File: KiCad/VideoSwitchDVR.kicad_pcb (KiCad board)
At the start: 2 copper layers, 18 x 25 mm, 7 parts, among them SW1 Joystick, U1 ATTINY84-20MU, U2 MAX4624/5

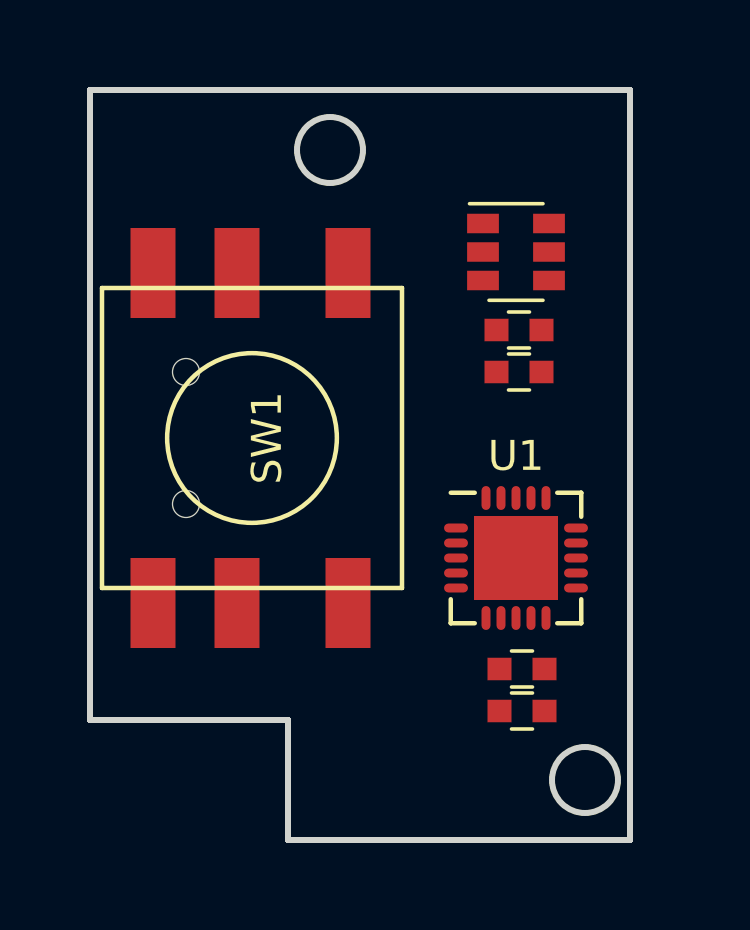
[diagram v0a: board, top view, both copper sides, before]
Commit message: Some progress on PCB. MCU changed to simplier one
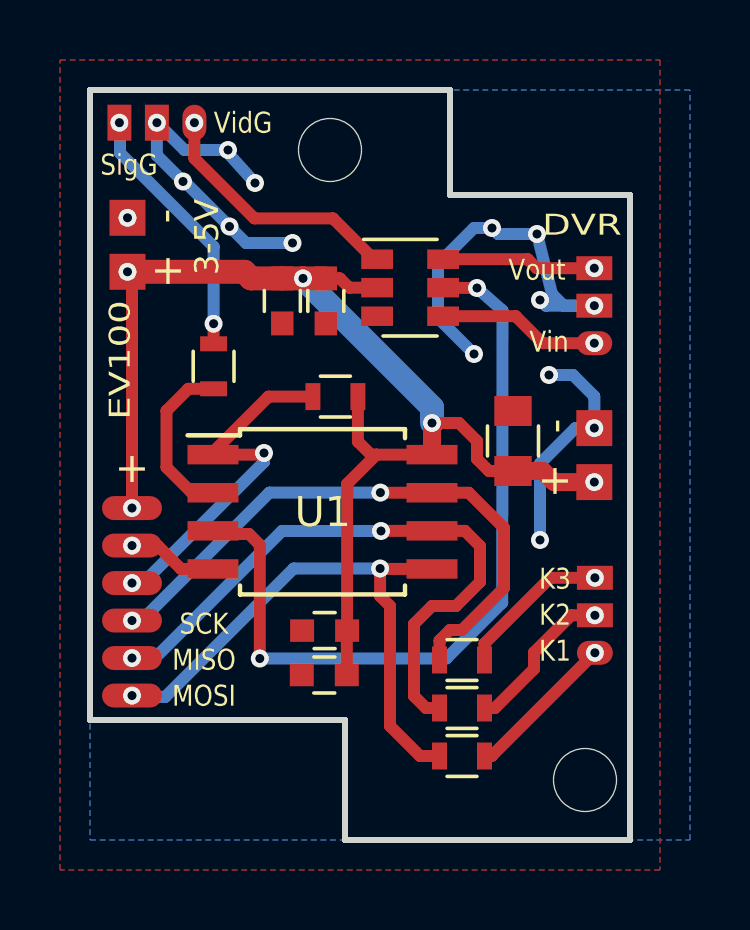
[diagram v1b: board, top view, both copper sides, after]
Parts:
- removed SW1: Joystick, KiCadCustomLibs:5dir6pin10x10mm_Joystick
- added C5: 22uf, Capacitors_SMD:C_0805, F.Cu at (114.1, 91.7)
- added J1: EV100, KiCadCustomLibs:USB_3_PADS, F.Cu at (102.2, 81.1)
- added J2: Buttons, KiCadCustomLibs:USB_3_PADS, F.Cu at (116.8, 97.5)
- added J3: DVR_VIDEO, KiCadCustomLibs:USB_3_PADS, F.Cu at (116.8, 87.2)
- added J4: PWR, KiCadCustomLibs:POWER2PIN, F.Cu at (101.2, 85.2)
- added J5: PWR_DVR, KiCadCustomLibs:POWER2PIN, F.Cu at (116.8, 92.2)
- added J6: PROG, KiCadCustomLibs:Pads_prog_6pin1.25mm, F.Cu at (101.4, 97.1)
- added R1: 100, Resistors_SMD:R_0603, F.Cu at (112.4, 102.2)
- added R2: 100, Resistors_SMD:R_0603, F.Cu at (112.4, 100.6)
- added R3: 100, Resistors_SMD:R_0603, F.Cu at (112.4, 99.0)
- added R4: 100, Resistors_SMD:R_0603, F.Cu at (104.1, 89.2)
- added R5: 10K, Resistors_SMD:R_0603, F.Cu at (108.2, 90.2)
- added REF**: MountingHole_2.2mm_M2, Mounting_Holes:MountingHole_2.2mm_M2, F.Cu at (108.0, 82.0)
- added REF**: MountingHole_2.2mm_M2, Mounting_Holes:MountingHole_2.2mm_M2, F.Cu at (116.5, 103.0)
- U1: value ATTINY84-20MU -> ATTINY15-1SC; footprint Housings_DFN_QFN:UQFN-20-1EP_4x4mm_Pitch0.5mm -> Housings_SOIC:SOIJ-8_5.3x5.3mm_Pitch1.27mm
- moved C4 8.24 mm to (106.4, 87.0), turned to 270 degrees
- moved C1 6.70 mm to (107.8, 98.0)
- moved C2 6.70 mm to (107.8, 99.5)
- moved U1 6.63 mm to (107.8, 94.1)
- moved C3 6.51 mm to (107.9, 87.0), turned to 270 degrees
- moved U2 3.73 mm to (110.7, 86.6)
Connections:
- C3 pad 1: Net-(C3-Pad1) -> VCC
- C4 pad 1: Net-(C3-Pad1) -> VCC
- U1 pad 1: Net-(U1-Pad1) -> /RST
- U1 pad 3: Net-(U1-Pad3) -> /VID_SWITCH
- U1 pad 4: Net-(U1-Pad4) -> GND
- U1 pad 5: Net-(U1-Pad5) -> /MOSI
- U1 pad 6: (no net) -> /MISO
- U1 pad 7: (no net) -> /SCK
- U1 pad 8: GND -> VCC
- U2 pad 2: Net-(C3-Pad1) -> VCC
- U2 pad 5: Net-(U1-Pad5) -> /VID_SWITCH
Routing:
- net VCC: track 0.00 -> 42.7 mm, vias 0 -> 5
- net GND: track 0.00 -> 34.8 mm, vias 0 -> 16
- net /VID_SWITCH: track 0.00 -> 26.4 mm, vias 0 -> 2
- net /MISO: track 0.00 -> 21.0 mm, vias 0 -> 2
- net /SCK: track 0.00 -> 20.2 mm, vias 0 -> 2
- net /MOSI: track 0.00 -> 19.2 mm, vias 0 -> 2
- net /RST: track 0.00 -> 12.3 mm, vias 0 -> 2
- net Net-(J1-Pad1): track 0.00 -> 8.70 mm, vias 0 -> 1
- net /VID_SENSE: track 0.00 -> 8.67 mm, vias 0 -> 2
- net Net-(R4-Pad2): track 0.00 -> 5.66 mm
- net Net-(J3-Pad1): track 0.00 -> 5.43 mm, vias 0 -> 1
- net /K2: track 0.00 -> 5.31 mm, vias 0 -> 1
- net Net-(J3-Pad3): track 0.00 -> 5.18 mm, vias 0 -> 1
- net /K3: track 0.00 -> 5.16 mm, vias 0 -> 1
- net /K1: track 0.00 -> 5.13 mm, vias 0 -> 1
- added copper zone on B.Cu, net GND
- added copper zone on F.Cu, net GND
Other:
- outline, holes or cut-outs redrawn
- net class Default: trace_width 0.25 -> 0.4; via_drill 0.4 -> 0.3
- rule pad_to_mask_clearance: 0.2 -> 0.1
- board text added: "+"
- board text added: "-"
- board text added: "3-5V"
- board text added: "DVR"
- board text added: "EV100"
- board text added: "K1"
- board text added: "K2"
- board text added: "K3"
- board text added: "MISO"
- board text added: "MOSI"
- board text added: "SCK"
- board text added: "SigG"
- board text added: "VidG"
- board text added: "Vin"
- board text added: "Vout"
- board text added: "When connected to google's power, don't connect power from programmer."
- board text added: "nppc 2018"

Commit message: Some work
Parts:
- added D1: B5819WS, Diodes_SMD:D_SOD-323, F.Cu at (102.5, 89.1)
- added JP1: VCC_SENSE, Resistors_SMD:R_0201_NoSilk, F.Cu at (112.4, 103.1)
- added Q1: AO3415 (P), TO_SOT_Packages_SMD:SOT-23, F.Cu at (115.9, 94.8)
- added R6: 1K, Resistors_SMD:R_0603, F.Cu at (113.2, 94.4)
- J2: footprint KiCadCustomLibs:USB_3_PADS -> KiCadCustomLibs:POWER2PIN
- R2: value 100 -> 100K
- moved R2 10.4 mm to (112.0, 90.2), turned to 0 degrees
- moved J5 1.17 mm to (116.8, 91.0)
- moved J2 0.99 mm to (116.9, 98.5), turned to 270 degrees
- moved C5 0.92 mm to (114.3, 90.8)
- moved R3 0.80 mm to (112.4, 99.8)
- moved R1 0.73 mm to (112.4, 101.5)
- moved J3 0.29 mm to (116.8, 86.9)
- moved R4 0.27 mm to (104.4, 89.2)
- moved C4 0.11 mm to (106.3, 87.0)
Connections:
- C5 pad 1: VCC -> Net-(C5-Pad1)
- J2 pad 1: /K1 -> /B2
- J2 pad 2: /K2 -> /B0
- J4 pad 1: VCC -> Net-(D1-Pad2)
- J5 pad 1: VCC -> Net-(C5-Pad1)
- R1 pad 1: /K1 -> /B0
- R2 pad 1: /K2 -> VCC
- R2 pad 2: /MISO -> Net-(Q1-Pad1)
- R3 pad 1: /K3 -> /B2
- U2 pad 1: Net-(J1-Pad1) -> /VID_SWITCH
- U2 pad 5: /VID_SWITCH -> Net-(J1-Pad1)
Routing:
- net GND: track 34.8 -> 51.6 mm, vias 16 -> 24
- net VCC: track 42.7 -> 53.7 mm
- net /VID_SWITCH: track 26.4 -> 16.7 mm, vias 2 -> 4
- net /MISO: track 21.0 -> 13.7 mm
- net /B0: track 0.00 -> 6.65 mm, vias 0 -> 1
- net Net-(J1-Pad1): track 8.70 -> 14.2 mm, vias 1 -> 2
- net Net-(C5-Pad1): track 0.00 -> 5.48 mm, vias 0 -> 1
- net Net-(Q1-Pad1): track 0.00 -> 5.40 mm
- net /K2: track 5.31 -> 0.00 mm, vias 1 -> 0
- net /K3: track 5.16 -> 0.00 mm, vias 1 -> 0
- net /K1: track 5.13 -> 0.00 mm, vias 1 -> 0
- net /B2: track 0.00 -> 5.06 mm, vias 0 -> 1
- net /SCK: track 20.2 -> 23.6 mm, vias 2 -> 4
- net Net-(D1-Pad2): track 0.00 -> 2.89 mm, vias 0 -> 1
- net /RST: track 12.3 -> 11.1 mm
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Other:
- outline, holes or cut-outs redrawn
- board text added: "B0"
- board text added: "B2"
- board text added: "V_SENSE"
- board text removed: "K1"
- board text removed: "K2"
- board text removed: "K3"
- board text removed: "When connected to google's power, don't connect power from programmer."

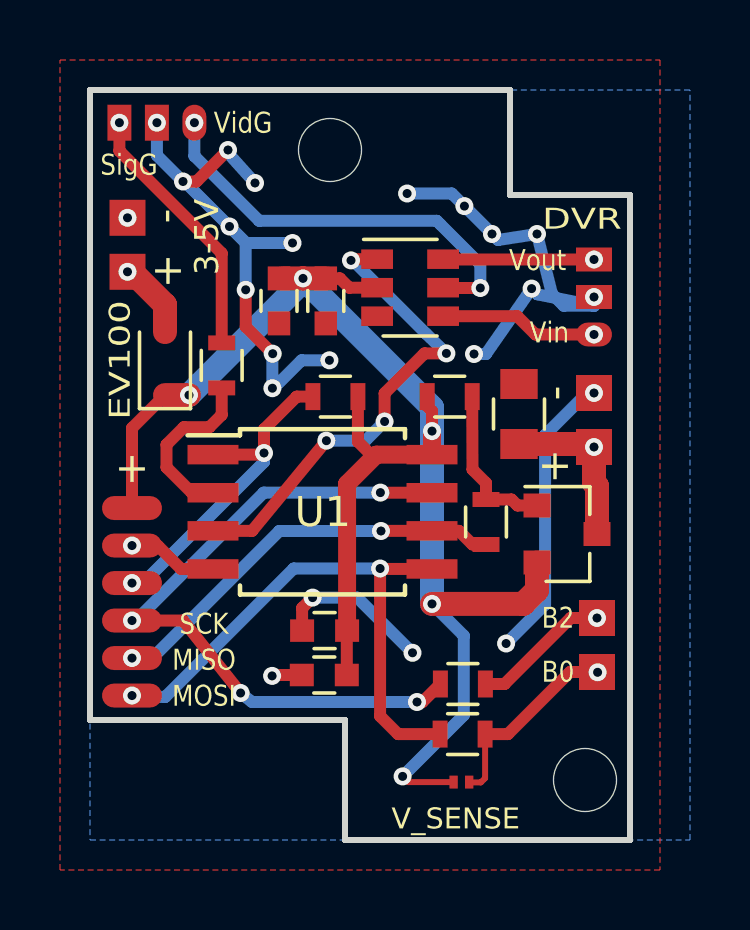
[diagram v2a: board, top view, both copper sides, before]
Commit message: Now can use two buttons and power loss sensing at the same time
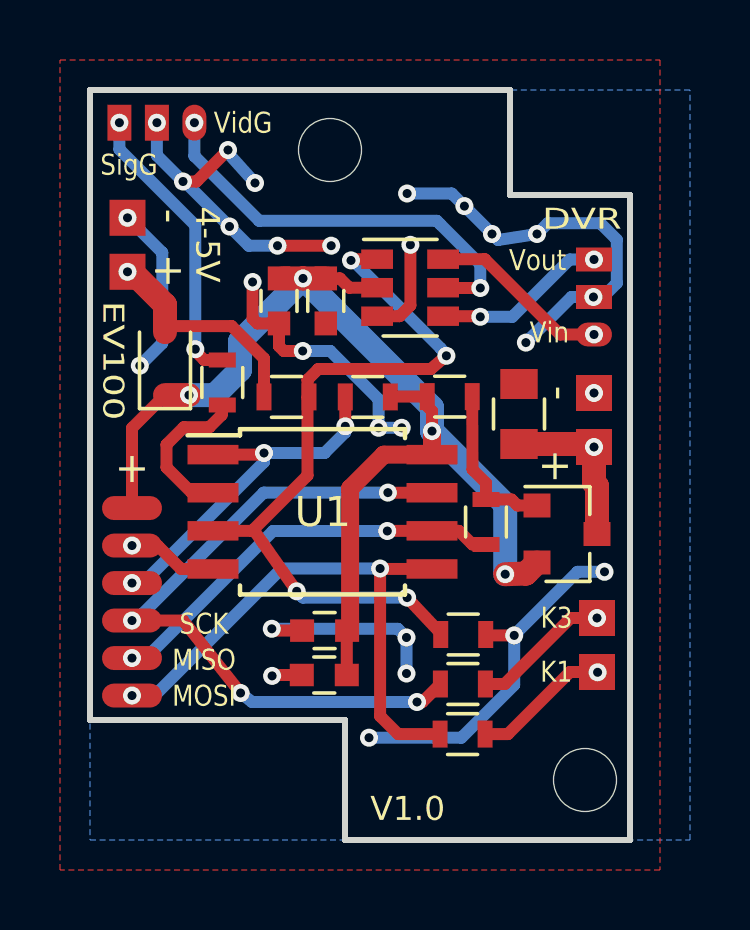
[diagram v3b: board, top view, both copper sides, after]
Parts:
- removed JP1: VCC_SENSE, Resistors_SMD:R_0201_NoSilk
- added R7: 4.7K, Resistors_SMD:R_0603, F.Cu at (106.5, 90.2)
- added R8: 47K, Resistors_SMD:R_0603, F.Cu at (112.4, 98.2)
- moved R5 1.08 mm to (109.3, 90.2)
- moved R4 0.57 mm to (104.4, 89.8)
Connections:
- net /B0 renamed /K1
- net /B2 renamed /K3
- net Net-(D1-Pad2) renamed +5V
- U2 pad 4: Net-(J3-Pad1) -> Net-(J3-Pad3)
- U2 pad 6: Net-(J3-Pad3) -> Net-(J3-Pad1)
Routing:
- net GND: track 51.6 -> 65.9 mm, vias 24 -> 29
- net VCC: track 53.7 -> 40.8 mm, vias 5 -> 4
- net /VID_SWITCH: track 16.7 -> 25.7 mm
- net +5V: track 2.89 -> 8.02 mm
- net /K1: track 6.65 -> 4.59 mm
- net /RST: track 11.1 -> 12.4 mm, vias 2 -> 3
- net /VID_SENSE: track 8.78 -> 10.0 mm, vias 1 -> 2
- net Net-(J3-Pad1): track 5.28 -> 6.08 mm
- net Net-(J3-Pad3): track 5.03 -> 5.83 mm, vias 1 -> 2
- net Net-(R4-Pad2): track 5.81 -> 5.24 mm
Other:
- board text added: "4-5V"
- board text added: "K1"
- board text added: "K3"
- board text added: "V1.0"
- board text removed: "3-5V"
- board text removed: "B0"
- board text removed: "B2"
- board text removed: "V_SENSE"

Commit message: PCB 2.0. Case SCAD.
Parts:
- removed R1, R3: 100, Resistors_SMD:R_0603
- removed R5: 10K, Resistors_SMD:R_0603
- removed REF** (x2): MountingHole_2.2mm_M2, Mounting_Holes:MountingHole_2.2mm_M2
- added J7: SuperCap, KiCadCustomLibs:ESC_PWR_PAD, F.Cu at (113.0, 81.5)
- U1: value ATTINY15-1SC -> ATTINY25
- moved J1 16.9 mm to (116.9, 89.4), turned to 90 degrees
- moved J6 16.2 mm to (105.0, 81.3), turned to 180 degrees
- moved J4 15.7 mm to (116.9, 85.4)
- moved C2 15.2 mm to (102.1, 85.4), turned to 90 degrees
- moved R2 11.9 mm to (110.7, 102.0)
- moved C1 11.2 mm to (102.1, 88.4), turned to 270 degrees
- moved R6 10.9 mm to (102.3, 94.3), turned to 270 degrees
- moved D1 10.0 mm to (111.1, 84.0), turned to 0 degrees
- moved U2 8.22 mm to (111.1, 94.8)
- moved C5 8.15 mm to (114.1, 99.0)
- moved J3 8.00 mm to (116.9, 94.9)
- moved J5 7.85 mm to (116.9, 98.8)
- moved C4 7.67 mm to (106.5, 94.7)
- moved C3 7.64 mm to (108.0, 94.7)
- moved U1 7.01 mm to (105.9, 87.3), turned to 90 degrees
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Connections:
- J2 pad 1: /K3 -> /SCK
- J2 pad 2: /K1 -> /MOSI
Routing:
- net GND: track 65.9 -> 43.4 mm, vias 29 -> 20
- net /VID_SWITCH: track 25.7 -> 8.19 mm, vias 4 -> 0
- net VCC: track 40.8 -> 55.4 mm, vias 4 -> 6
- net /MOSI: track 19.0 -> 31.3 mm, vias 2 -> 3
- net Net-(Q1-Pad1): track 5.40 -> 14.3 mm
- net /SCK: track 23.6 -> 31.2 mm, vias 4 -> 2
- net /K3: track 5.06 -> 0.00 mm, vias 1 -> 0
- net Net-(J1-Pad1): track 14.2 -> 9.29 mm
- net /K1: track 4.59 -> 0.00 mm, vias 1 -> 0
- net +5V: track 8.02 -> 12.2 mm
- net /VID_SENSE: track 10.0 -> 6.14 mm
- net /RST: track 12.4 -> 9.80 mm, vias 3 -> 2
- net Net-(R4-Pad2): track 5.24 -> 7.15 mm
- net /MISO: track 13.7 -> 15.2 mm, vias 2 -> 3
- net Net-(J3-Pad1): track 6.08 -> 5.65 mm, vias 1 -> 2
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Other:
- board size 18 x 25 mm -> 16.9 x 24.5 mm
- board text added: "5V"
- board text added: "RST"
- board text added: "Super Cap+"
- board text added: "V2.0"
- board text removed: "4-5V"
- board text removed: "V1.0"
